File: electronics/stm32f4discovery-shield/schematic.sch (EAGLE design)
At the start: 43 parts, among them IC1 MAX3468CPA, IC3 LM340H-12, IC4 LM340H-12, J1 POWER_JACKSLT, Q1 BC548

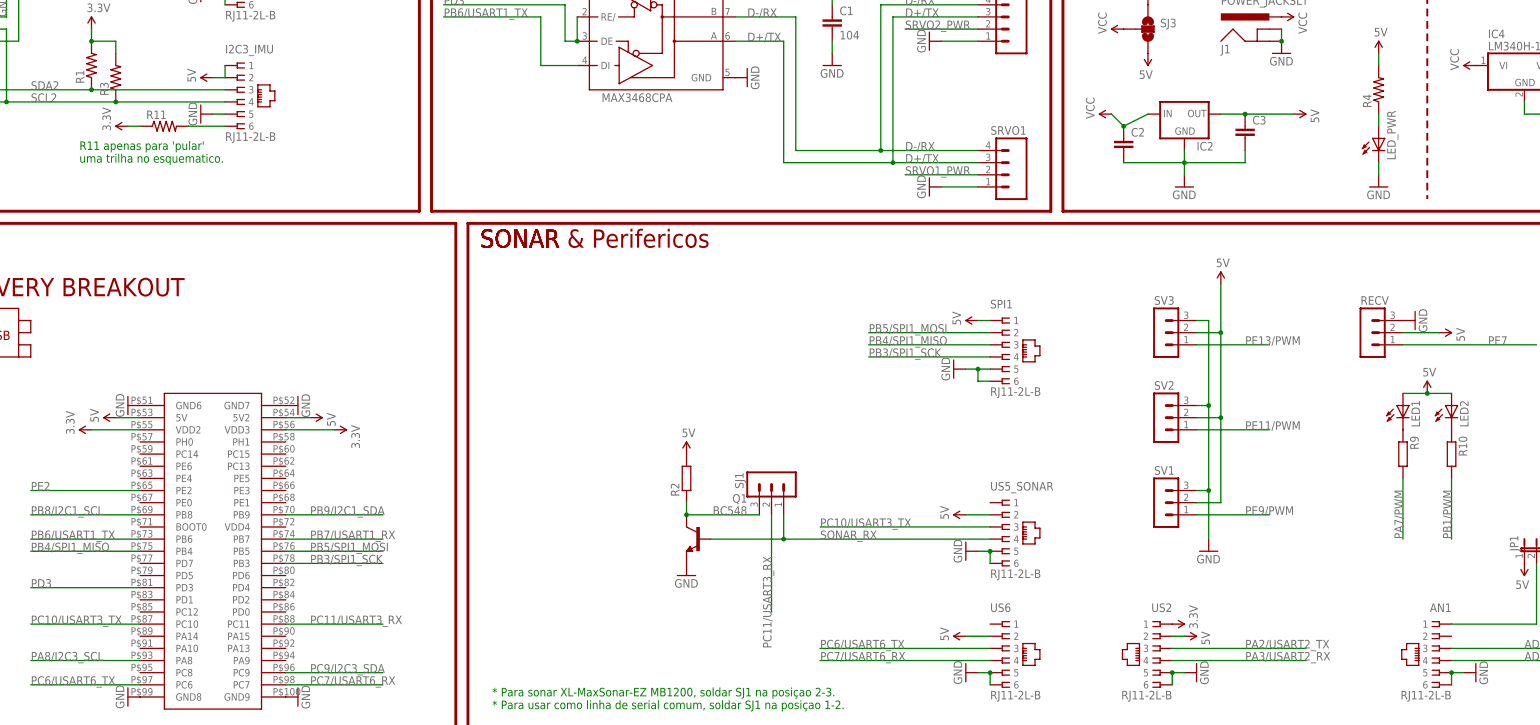
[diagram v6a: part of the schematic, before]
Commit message: Correcoes finais a placa.
- Conectores RECV, SV1, SV2 e SV3 movidos mais para a borda da placa.
- 5V disponiveis no pino 2 do conector US6.
- Conector US5_SONAR renomeado para US3_SONAR (por usar a USART3)
- No conector I2C3_IMU, GND disponivel agora no pino 2 e 3v3 no pino 1.
- Pino de GND do MAX485 ok (antes desconectado da malha de terra).
- GND disponivel nos pinos 5 e 6 do conector US3_SONAR.

	modified:   electronics/stm32f4discovery-shield/schematic.brd
	modified:   electronics/stm32f4discovery-shield/schematic.sch
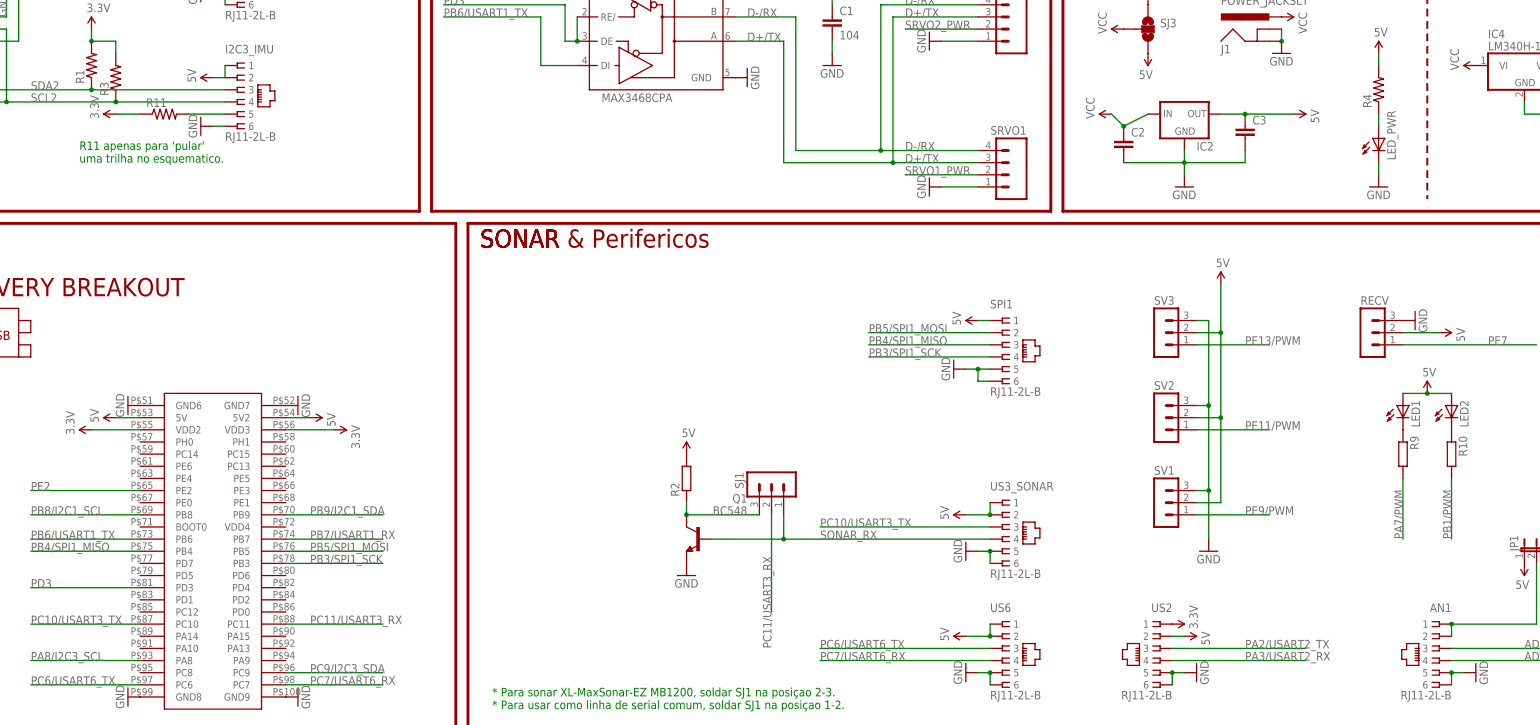
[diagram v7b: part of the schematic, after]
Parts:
- renumbered US5_SONAR to US3_SONAR
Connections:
- net 5V: now also US3_SONAR.1, US6.1
- net GND: now also I2C3_IMU.6; no longer I2C3_IMU.5
- net N$10: now also AN1.2
- net N$9: now also I2C3_IMU.5; no longer I2C3_IMU.6
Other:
- moved on the sheet: R11
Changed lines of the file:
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@@
 <part name="SUPPLY12" library="SparkFun-Aesthetics" deviceset="5V" device=""/>
 <part name="GND19" library="SparkFun-Aesthetics" deviceset="GND" device=""/>
-<part name="US5_SONAR" library="con-tycoelectronics" deviceset="RJ11" device="" technology="-2L-B"/>
+<part name="US3_SONAR" library="con-tycoelectronics" deviceset="RJ11" device="" technology="-2L-B"/>
 <part name="Q1" library="transistor-npn" deviceset="BC548*" device=""/>
 <part name="GND20" library="SparkFun-Aesthetics" deviceset="GND" device=""/>
@@
 <instance part="I2C1_ESC" gate="G$1" x="132.08" y="160.02"/>
 <instance part="I2C3_IMU" gate="G$1" x="132.08" y="134.62"/>
-<instance part="GND11" gate="1" x="124.46" y="129.54" rot="R270"/>
+<instance part="GND11" gate="1" x="124.46" y="127" rot="R270"/>
 <instance part="SUPPLY5" gate="G$1" x="127" y="137.16" rot="R90"/>
-<instance part="SUPPLY6" gate="G$1" x="109.22" y="127" rot="R90"/>
+<instance part="SUPPLY6" gate="G$1" x="106.68" y="129.54" rot="R90"/>
 <instance part="SUPPLY8" gate="G$1" x="127" y="162.56" rot="R90"/>
 <instance part="GND12" gate="1" x="124.46" y="154.94" rot="R270"/>
@@
 <instance part="SUPPLY12" gate="G$1" x="287.02" y="86.36" rot="R90"/>
 <instance part="GND19" gate="1" x="281.94" y="76.2" rot="R270"/>
-<instance part="US5_SONAR" gate="G$1" x="292.1" y="43.18"/>
+<instance part="US3_SONAR" gate="G$1" x="292.1" y="43.18"/>
 <instance part="Q1" gate="G$1" x="228.6" y="40.64" rot="MR0"/>
 <instance part="GND20" gate="1" x="284.48" y="38.1" rot="R270"/>
@@
 <instance part="SV4" gate="1" x="48.26" y="124.46" rot="R270"/>
 <instance part="SUPPLY7" gate="G$1" x="327.66" y="22.86" rot="MR90"/>
-<instance part="R11" gate="G$1" x="116.84" y="127"/>
+<instance part="R11" gate="G$1" x="116.84" y="129.54"/>
 <instance part="AN1" gate="G$1" x="383.54" y="17.78" rot="MR0"/>
 <instance part="GND18" gate="1" x="391.16" y="12.7" rot="R90"/>
@@
 </segment>
 <segment>
-<pinref part="I2C3_IMU" gate="G$1" pin="5"/>
-<pinref part="GND11" gate="1" pin="GND"/>
-<wire x1="127" y1="129.54" x2="129.54" y2="129.54" width="0.1524" layer="91"/>
-</segment>
-<segment>
 <pinref part="I2C1_ESC" gate="G$1" pin="5"/>
 <pinref part="GND12" gate="1" pin="GND"/>
@@
 <segment>
 <pinref part="GND20" gate="1" pin="GND"/>
-<pinref part="US5_SONAR" gate="G$1" pin="5"/>
+<pinref part="US3_SONAR" gate="G$1" pin="5"/>
 <wire x1="287.02" y1="38.1" x2="289.56" y2="38.1" width="0.1524" layer="91"/>
-<pinref part="US5_SONAR" gate="G$1" pin="6"/>
+<pinref part="US3_SONAR" gate="G$1" pin="6"/>
 <wire x1="289.56" y1="35.56" x2="289.56" y2="38.1" width="0.1524" layer="91"/>
 <junction x="289.56" y="38.1"/>
@@
 <junction x="386.08" y="12.7"/>
 </segment>
+<segment>
+<pinref part="GND11" gate="1" pin="GND"/>
+<pinref part="I2C3_IMU" gate="G$1" pin="6"/>
+<wire x1="127" y1="127" x2="129.54" y2="127" width="0.1524" layer="91"/>
+</segment>
 </net>
 <net name="5V" class="0">
@@
 <segment>
 <pinref part="SUPPLY14" gate="G$1" pin="5V"/>
-<pinref part="US5_SONAR" gate="G$1" pin="2"/>
+<pinref part="US3_SONAR" gate="G$1" pin="2"/>
 <wire x1="284.48" y1="45.72" x2="289.56" y2="45.72" width="0.1524" layer="91"/>
+<pinref part="US3_SONAR" gate="G$1" pin="1"/>
+<wire x1="289.56" y1="48.26" x2="289.56" y2="45.72" width="0.1524" layer="91"/>
+<junction x="289.56" y="45.72"/>
 </segment>
 <segment>
@@
 <pinref part="SUPPLY17" gate="G$1" pin="5V"/>
 <wire x1="284.48" y1="20.32" x2="289.56" y2="20.32" width="0.1524" layer="91"/>
+<pinref part="US6" gate="G$1" pin="1"/>
+<wire x1="289.56" y1="22.86" x2="289.56" y2="20.32" width="0.1524" layer="91"/>
+<junction x="289.56" y="20.32"/>
 </segment>
 <segment>
@@
 <pinref part="SUPPLY6" gate="G$1" pin="3.3V"/>
 <pinref part="R11" gate="G$1" pin="1"/>
-<wire x1="109.22" y1="127" x2="111.76" y2="127" width="0.1524" layer="91"/>
+<wire x1="106.68" y1="129.54" x2="111.76" y2="129.54" width="0.1524" layer="91"/>
 </segment>
 <segment>
@@
 <net name="PC10/USART3_TX" class="0">
 <segment>
-<pinref part="US5_SONAR" gate="G$1" pin="3"/>
+<pinref part="US3_SONAR" gate="G$1" pin="3"/>
 <wire x1="289.56" y1="43.18" x2="254" y2="43.18" width="0.1524" layer="91"/>
 <label x="254" y="43.18" size="1.778" layer="95"/>
@@
 <net name="SONAR_RX" class="0">
 <segment>
-<pinref part="US5_SONAR" gate="G$1" pin="4"/>
+<pinref part="US3_SONAR" gate="G$1" pin="4"/>
 <wire x1="289.56" y1="40.64" x2="246.38" y2="40.64" width="0.1524" layer="91"/>
 <label x="254" y="40.64" size="1.778" layer="95"/>
@@
 </segment>
 </net>
-<net name="N$9" class="0">
-<segment>
-<pinref part="I2C3_IMU" gate="G$1" pin="6"/>
-<pinref part="R11" gate="G$1" pin="2"/>
-<wire x1="121.92" y1="127" x2="129.54" y2="127" width="0.1524" layer="91"/>
-</segment>
-</net>
 <net name="ADC1" class="0">
 <segment>
@@
 <wire x1="386.08" y1="22.86" x2="403.86" y2="22.86" width="0.1524" layer="91"/>
 <wire x1="403.86" y1="22.86" x2="403.86" y2="27.94" width="0.1524" layer="91"/>
+<pinref part="AN1" gate="G$1" pin="2"/>
+<wire x1="386.08" y1="20.32" x2="386.08" y2="22.86" width="0.1524" layer="91"/>
+<junction x="386.08" y="22.86"/>
 </segment>
 </net>
@@
 </segment>
 </net>
+<net name="N$9" class="0">
+<segment>
+<pinref part="R11" gate="G$1" pin="2"/>
+<pinref part="I2C3_IMU" gate="G$1" pin="5"/>
+<wire x1="121.92" y1="129.54" x2="129.54" y2="129.54" width="0.1524" layer="91"/>
+</segment>
+</net>
